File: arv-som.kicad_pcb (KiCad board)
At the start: 2 copper layers, 55 x 40 mm, 345 parts, among them J3 DF40C-100DP-0.4V(51), J4 DF40C-100DP-0.4V(51), Q1 BSS138AKA, Q2 BSS138AKA, Q3 BSS138AKA, Q4 BSS138AKA, U10 TDA19988BHN_C1,557, U11 KSZ9031RNXCA, U12 MT53E256M32D2DS-053, U13 VIC7100, U2 MT53E256M32D2, U5 LMR62014XMF_NOPB, U8 TPS65086100, U9 GD25LQ256DWIGR, Y1 ABM8G-25.000MHZ-18-D2Y-T

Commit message: Renamed design files
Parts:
- SP1, SP2, SP3, SP4: footprint riscv-u74-som-footprints:9774030151 -> arv-som-footprints:9774030151
- U2: footprint riscv-u74-som-footprints:BGA-200_10.0x14.5mm_Layout12x22_P0.80x0.65mm -> arv-som-footprints:BGA-200_10.0x14.5mm_Layout12x22_P0.80x0.65mm
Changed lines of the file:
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@@
     )
   )
-  (module riscv-u74-som-footprints:9774030151 (layer F.Cu)
+  (module arv-som-footprints:9774030151 (layer F.Cu)
     (at 181.520001 91.470002)
     (fp_text reference SP4 (at 0 -4.2) (layer F.SilkS)
@@
     )
   )
-  (module riscv-u74-som-footprints:9774030151 (layer F.Cu)
+  (module arv-som-footprints:9774030151 (layer F.Cu)
     (at 133.520001 91.470002)
     (fp_text reference SP3 (at 0 -4.2) (layer F.SilkS)
@@
     )
   )
-  (module riscv-u74-som-footprints:9774030151 (layer F.Cu)
+  (module arv-som-footprints:9774030151 (layer F.Cu)
     (at 181.520001 58.470002)
     (fp_text reference SP2 (at 0 -4.2) (layer F.SilkS)
@@
     )
   )
-  (module riscv-u74-som-footprints:9774030151 (layer F.Cu)
+  (module arv-som-footprints:9774030151 (layer F.Cu)
     (at 133.520001 58.470002)
     (fp_text reference SP1 (at 0 -4.2) (layer F.SilkS)
@@
     )
   )
-  (module riscv-u74-som-footprints:BGA-200_10.0x14.5mm_Layout12x22_P0.80x0.65mm (layer F.Cu)
+  (module arv-som-footprints:BGA-200_10.0x14.5mm_Layout12x22_P0.80x0.65mm (layer F.Cu)
     (at 175.620001 73.970002)
     (descr "BGA-200, 14.5x10.0mm, 200 Ball, 12x22 Layout, 0.8x0.65mm Pitch, http://www.issi.com/WW/pdf/43-46LQ32256A-AL.pdf")

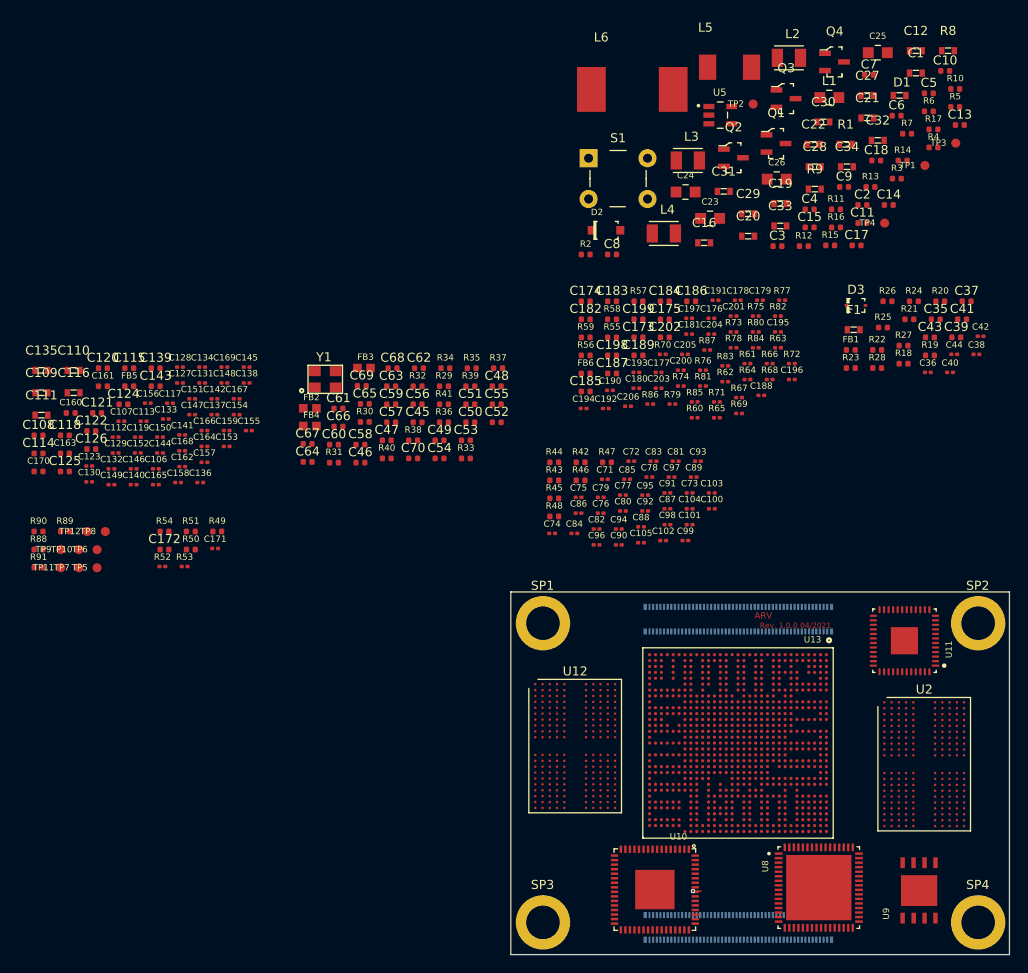
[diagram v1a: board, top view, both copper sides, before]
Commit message: Updated interfaces, CPU and B2B connector connections
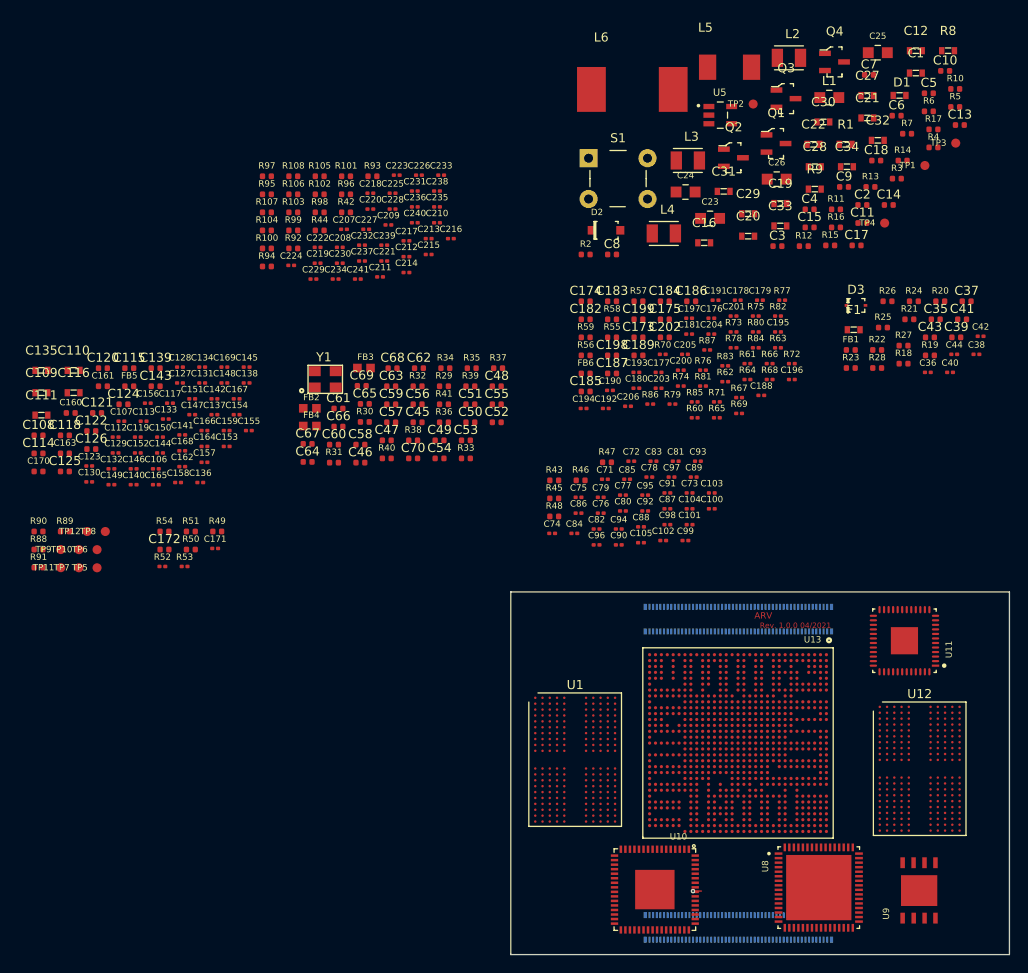
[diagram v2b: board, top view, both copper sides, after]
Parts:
- removed SP1, SP2, SP3, SP4: 9774030151, arv-som-footprints:9774030151
- removed U2: MT53E256M32D2, arv-som-footprints:BGA-200_10.0x14.5mm_Layout12x22_P0.80x0.65mm
- added C207: C_100n_0201, antmicro-footprints:0201-res, F.Cu at (111.6, 15.0)
- added C208: C_100n_0201, antmicro-footprints:0201-res, F.Cu at (111.2, 17.0)
- added C209: C_100n_0201, antmicro-footprints:0201-res, F.Cu at (116.5, 14.5)
- added C210: C_100n_0201, antmicro-footprints:0201-res, F.Cu at (121.9, 14.3)
- added C211: C_100n_0201, antmicro-footprints:0201-res, F.Cu at (115.6, 20.2)
- added C212: C_100n_0201, antmicro-footprints:0201-res, F.Cu at (118.5, 18.0)
- added C213: C_100n_0201, antmicro-footprints:0201-res, F.Cu at (121.0, 16.0)
- added C214: C_100n_0201, antmicro-footprints:0201-res, F.Cu at (118.5, 19.7)
- added C215: C_100n_0201, antmicro-footprints:0201-res, F.Cu at (121.0, 17.8)
- added C216: C_100n_0201, antmicro-footprints:0201-res, F.Cu at (123.4, 16.0)
- added C217: C_100n_0201, antmicro-footprints:0201-res, F.Cu at (118.5, 16.2)
- added C218: C_100n_0201, antmicro-footprints:0201-res, F.Cu at (114.5, 11.0)
- added C219: C_100n_0201, antmicro-footprints:0201-res, F.Cu at (108.7, 18.7)
- added C220: C_100n_0201, antmicro-footprints:0201-res, F.Cu at (114.5, 12.7)
- added C221: C_100n_0201, antmicro-footprints:0201-res, F.Cu at (116.1, 18.5)
- added C222: C_100n_0201, antmicro-footprints:0201-res, F.Cu at (108.7, 17.0)
- added C223: C_100n_0201, antmicro-footprints:0201-res, F.Cu at (117.4, 9.00)
- added C224: C_100n_0201, antmicro-footprints:0201-res, F.Cu at (105.8, 19.0)
- added C225: C_100n_0201, antmicro-footprints:0201-res, F.Cu at (117.0, 11.0)
- added C226: C_100n_0201, antmicro-footprints:0201-res, F.Cu at (119.9, 9.00)
- added C227: C_100n_0201, antmicro-footprints:0201-res, F.Cu at (114.1, 15.0)
- added C228: C_100n_0201, antmicro-footprints:0201-res, F.Cu at (117.0, 12.7)
- added C229: C_100n_0201, antmicro-footprints:0201-res, F.Cu at (108.3, 20.5)
- added C230: C_100n_0201, antmicro-footprints:0201-res, F.Cu at (111.2, 18.7)
- added C231: C_100n_0201, antmicro-footprints:0201-res, F.Cu at (119.4, 10.8)
- added C232: C_100n_0201, antmicro-footprints:0201-res, F.Cu at (113.6, 16.7)
- added C233: C_100n_0201, antmicro-footprints:0201-res, F.Cu at (122.3, 9.00)
- added C234: C_100n_0201, antmicro-footprints:0201-res, F.Cu at (110.7, 20.5)
- added C235: C_100n_0201, antmicro-footprints:0201-res, F.Cu at (121.9, 12.5)
- added C236: C_100n_0201, antmicro-footprints:0201-res, F.Cu at (119.4, 12.5)
- added C237: C_100n_0201, antmicro-footprints:0201-res, F.Cu at (113.6, 18.5)
- added C238: C_100n_0201, antmicro-footprints:0201-res, F.Cu at (121.9, 10.8)
- added C239: C_100n_0201, antmicro-footprints:0201-res, F.Cu at (116.1, 16.7)
- added C240: C_100n_0201, antmicro-footprints:0201-res, F.Cu at (119.4, 14.3)
- added C241: C_100n_0201, antmicro-footprints:0201-res, F.Cu at (113.2, 20.5)
- added R100: R_0R_0402, antmicro-footprints:0402-res, F.Cu at (103.1, 17.1)
- added R101: R_10k_0402, antmicro-footprints:0402-res, F.Cu at (111.9, 9.12)
- added R102: R_0R_0402, antmicro-footprints:0402-res, F.Cu at (108.9, 11.1)
- added R103: R_10k_0402, antmicro-footprints:0402-res, F.Cu at (106.0, 13.1)
- added R104: R_10k_0402, antmicro-footprints:0402-res, F.Cu at (103.1, 15.1)
- added R105: R_10k_0402, antmicro-footprints:0402-res, F.Cu at (108.9, 9.12)
- added R106: R_10k_0402, antmicro-footprints:0402-res, F.Cu at (106.0, 11.1)
- added R107: R_10k_0402, antmicro-footprints:0402-res, F.Cu at (103.1, 13.1)
- added R108: R_10k_0402, antmicro-footprints:0402-res, F.Cu at (106.0, 9.12)
- added R92: R_10k_0402, antmicro-footprints:0402-res, F.Cu at (106.0, 17.1)
- added R93: R_10k_0402, antmicro-footprints:0402-res, F.Cu at (114.8, 9.12)
- added R94: R_10k_0402, antmicro-footprints:0402-res, F.Cu at (103.1, 19.1)
- added R95: R_10k_0402, antmicro-footprints:0402-res, F.Cu at (103.1, 11.1)
- added R96: R_10k_0402, antmicro-footprints:0402-res, F.Cu at (111.9, 11.1)
- added R97: R_240R_0402, antmicro-footprints:0402-res, F.Cu at (103.1, 9.12)
- added R98: R_10k_0402, antmicro-footprints:0402-res, F.Cu at (108.9, 13.1)
- added R99: R_240R_0402, antmicro-footprints:0402-res, F.Cu at (106.0, 15.1)
- added U1: MT53E256M32D2DS-053, antmicro-footprints:BGA-200_10.0x14.5mm_Layout12x22_P0.80x0.65mm, F.Cu at (137.1, 73.5)
- R42: value R_10k_0402 -> R_240R_0402
- moved U12 38.1 mm to (175.1, 74.5)
- moved R42 37.8 mm to (111.9, 13.1)
- moved R44 36.4 mm to (108.9, 15.1)
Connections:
- net ETH_INT_N renamed Net-(U11-Pad38)
- net ETH_MDC renamed RGMII_MDC
- net ETH_nLED1 renamed Net-(J3-Pad19)
- net FNSH028_HDMI_I2S_TX0 renamed HDMI_I2S_TX0
- net Net-(R44-Pad2) renamed DDR0_ODT_1
- net RGMII_REF_CLK renamed LED_MODE
- net RGMII_RX_CLK renamed RGMII_RXCLK
- net RGMII_RX_DV renamed RGMII_RXDV
- net RGMII_TX_CLK renamed RGMII_GTXCLK
- net SYNC_IN renamed Net-(J3-Pad16)
- net SYNC_OUT renamed Net-(J3-Pad18)
- J4 pad 57: DSI0_D0_N -> CDTX_DSI_D0_N
- J4 pad 59: DSI0_D0_P -> CDTX_DSI_D0_P
- J4 pad 63: DSI0_D1_N -> CDTX_DSI_D1_N
- J4 pad 65: DSI0_D1_P -> CDTX_DSI_D1_P
- J4 pad 69: DSI0_C_N -> CDTX_DSI_D2_N
- J4 pad 71: DSI0_C_P -> CDTX_DSI_D2_P
- R39 pad 1: ETH_LED1 -> ETH_LED2
- R40 pad 1: ETH_LED2 -> ETH_LED1
- R42 pad 1: CS0_B -> Net-(R42-Pad1)
- R42 pad 2: GND -> VDDQ
- R45 pad 2: GND -> VDDQ
- R46 pad 2: OTD_CA_A -> DDR0_ODT_0
- R48 pad 2: RESET_N -> DDR0_RSTN
- U10 pad 23: FNSH026_HDMI_BCLK -> HDMI_BCLK
- U10 pad 24: FNSH027_HDMI_I2S_LRCLK -> HDMI_LRCLK
- U10 pad 27: FNSH025_HDMI_12MHZ -> HDMI_12MHZ
- U10 pad 50: FNSH032_HDMI_INT -> HDMI_INT
- U10 pad 51: FNSH061_I2C0_SDA -> I2C0_SDA
- U10 pad 52: FNSH062_I2C0_SCL -> I2C0_SCL
- U11 pad 25: RGMII_TX_DV -> RGMII_TXEN
- U11 pad 37: ETH_MDIO -> RGMII_MDIO
- U12 pad A8: Net-(U12-PadA8) -> Net-(R42-Pad1)
- U12 pad AA11: Net-(U12-PadAA11) -> DDR0_DQ24
- U12 pad AA2: Net-(U12-PadAA2) -> DDR0_DQ16
- U12 pad AA4: Net-(U12-PadAA4) -> DDR0_DQ23
- U12 pad AA9: Net-(U12-PadAA9) -> DDR0_DQ31
- U12 pad B11: DQ08_A -> DDR0_DQ08
- U12 pad B2: DQ00_A -> DDR0_DQ00
- U12 pad B4: DQ07_A -> DDR0_DQ07
- U12 pad B9: DQ15_A -> DDR0_DQ15
- U12 pad C10: DMI_1A -> DDR0_DMI1
- U12 pad C11: DQ09_A -> DDR0_DQ09
- U12 pad C2: DQ01_A -> DDR0_DQ01
- U12 pad C3: DMI_0A -> DDR0_DMI0
- U12 pad C4: DQ06_A -> DDR0_DQ06
- U12 pad C9: DQ14_A -> DDR0_DQ14
- U12 pad D10: DQ_S1_TA -> DDR0_DQS1N
- U12 pad D3: DQ_S0_TA -> DDR0_DQS0N
- U12 pad E10: DQ_S1_CA -> DDR0_DQS1P
- U12 pad E11: DQ10_A -> DDR0_DQ10
- U12 pad E2: DQ02_A -> DDR0_DQ02
- U12 pad E3: DQ_S0_CA -> DDR0_DQS0P
- U12 pad E4: DQ05_A -> DDR0_DQ05
- U12 pad E9: DQ13_A -> DDR0_DQ13
- U12 pad F11: DQ11_A -> DDR0_DQ11
- U12 pad F2: DQ03_A -> DDR0_DQ03
- U12 pad F4: DQ04_A -> DDR0_DQ04
- U12 pad F9: DQ12_A -> DDR0_DQ12
- U12 pad H3: Net-(U12-PadH3) -> DDR0_CS1
- U12 pad H4: CS0_A -> DDR0_CS0
- U12 pad J5: Net-(U12-PadJ5) -> DDR0_CKE1
- U12 pad P4: DDR0_CKE1 -> DDR0_CKE0
- U12 pad P5: Net-(U12-PadP5) -> DDR0_CKE1
- U12 pad R3: Net-(U12-PadR3) -> DDR0_CS3
- U12 pad R4: CS0_B -> DDR0_CS2
- U12 pad U11: Net-(U12-PadU11) -> DDR0_DQ27
- U12 pad U2: Net-(U12-PadU2) -> DDR0_DQ19
- U12 pad U4: Net-(U12-PadU4) -> DDR0_DQ20
- U12 pad U9: Net-(U12-PadU9) -> DDR0_DQ28
- U12 pad V10: Net-(U12-PadV10) -> DDR0_DQS3P
- U12 pad V11: Net-(U12-PadV11) -> DDR0_DQ26
- U12 pad V2: Net-(U12-PadV2) -> DDR0_DQ18
- U12 pad V3: Net-(U12-PadV3) -> DDR0_DQS2P
- U12 pad V4: Net-(U12-PadV4) -> DDR0_DQ21
- U12 pad V9: Net-(U12-PadV9) -> DDR0_DQ29
- U12 pad W10: Net-(U12-PadW10) -> DDR0_DQS3N
- U12 pad W3: Net-(U12-PadW3) -> DDR0_DQS2N
- U12 pad Y10: Net-(U12-PadY10) -> DDR0_DMI3
- U12 pad Y11: Net-(U12-PadY11) -> DDR0_DQ25
- U12 pad Y2: Net-(U12-PadY2) -> DDR0_DQ17
- U12 pad Y3: Net-(U12-PadY3) -> DDR0_DMI2
- U12 pad Y4: Net-(U12-PadY4) -> DDR0_DQ22
- U12 pad Y9: Net-(U12-PadY9) -> DDR0_DQ30
- U13 pad AB30: GMAC_TXEN -> RGMII_TXEN
- U13 pad Y29: ETH_MDIO -> RGMII_MDIO

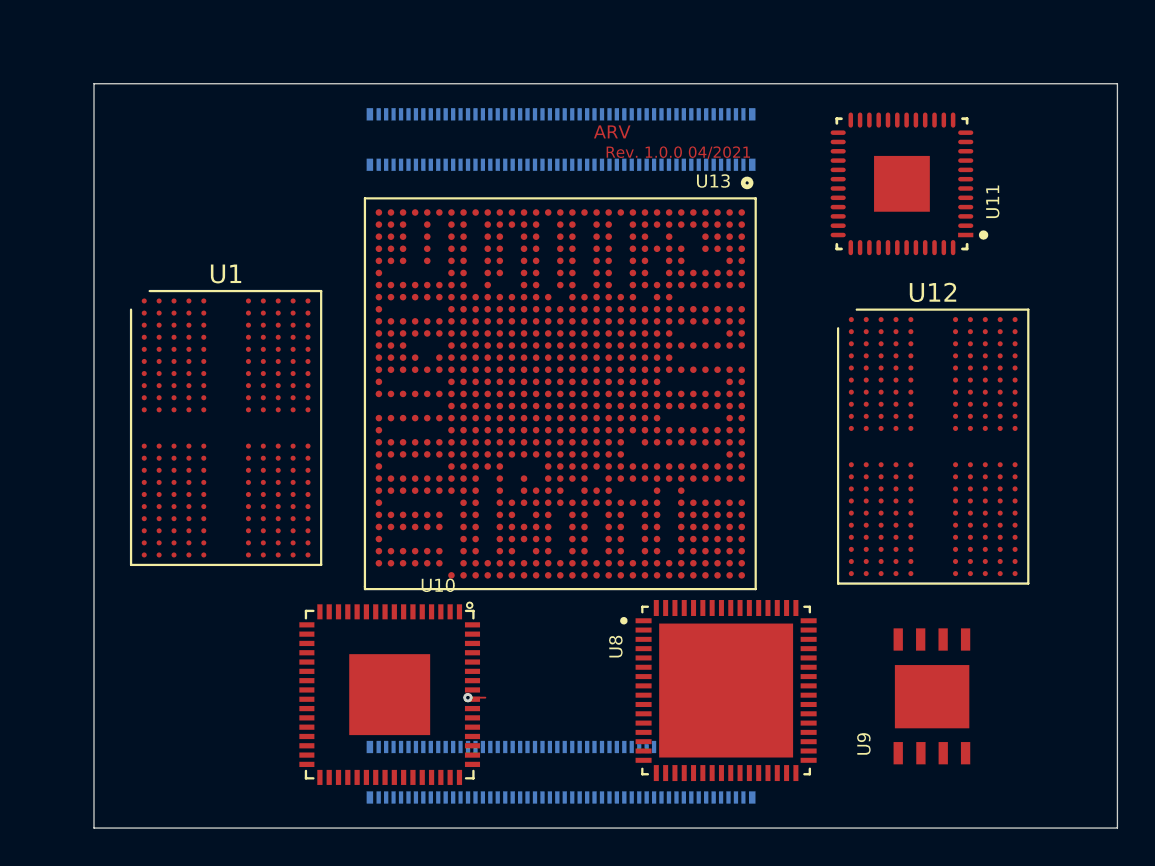
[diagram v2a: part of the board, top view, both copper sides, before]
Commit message: Added logotypes
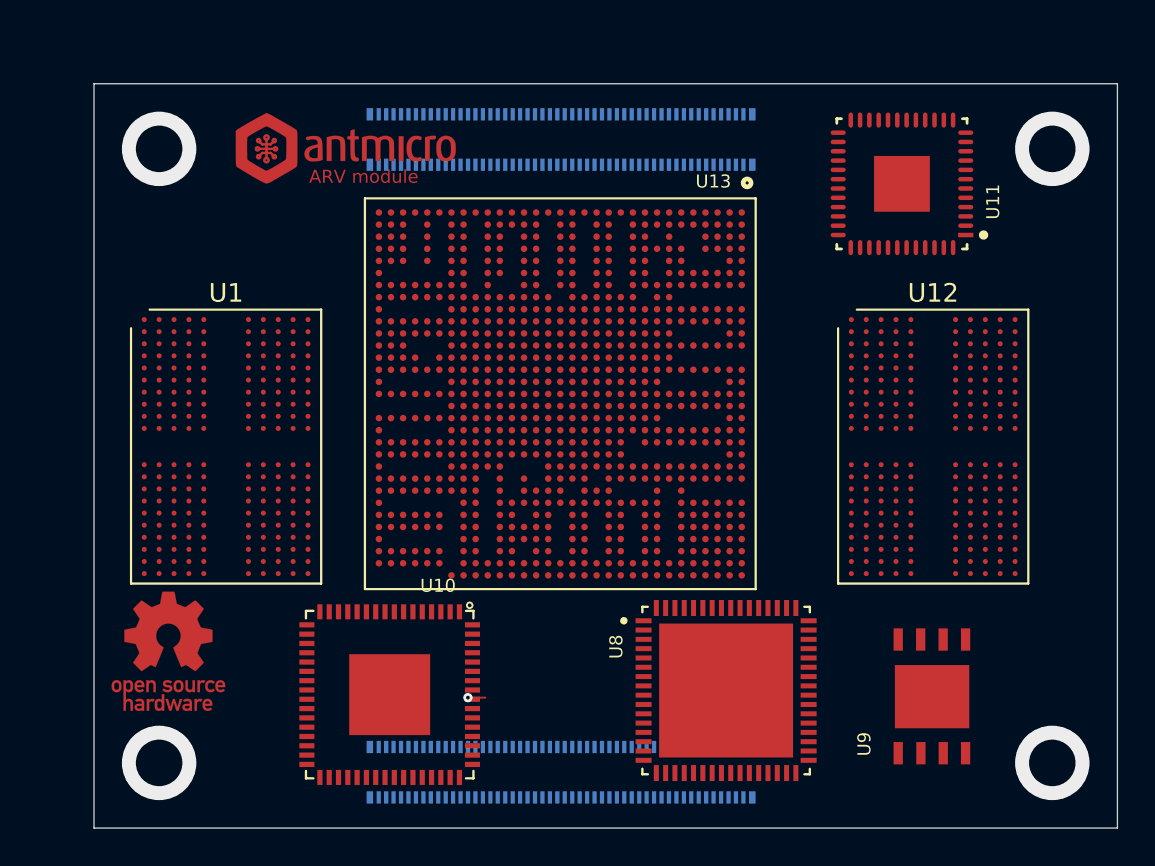
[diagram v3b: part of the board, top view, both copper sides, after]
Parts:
- added N1: antmicro_logo, antmicro-footprints:antmicro-logo_scaled_12mm, F.Cu at (143.5, 58.5)
- added N2: oshw_logo, antmicro-footprints:oshw-logo, F.Cu at (134.0, 85.5)
- moved U1 1.00 mm to (137.1, 74.5)
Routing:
- net (no net): vias 0 -> 4
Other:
- board text added: "ARV module"
- board text removed: "ARV"
- board text removed: "Rev. 1.0.0 04/2021"

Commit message: Minor mock update
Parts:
- removed C1, C16, C27, C28: C_10u_0603, antmicro-footprints:0603-cap
- removed C10, C13, C17, C18: C_100n_0402_16V, antmicro-footprints:0402-cap
- removed C100, C101, C102, C103, C104, C105, C106, C107, C112, C113, C117, C119, C123, C127, C128, C129, C130, C131, C132, C133, C134, C136, C137, C138, C140, C141, C142, C144, C145, C146, C147, C148, C149, C150, C151, C152, C153, C154, C155, C156, C157, C158, C159, C162, C164, C165, C166, C167, C168, C169, C171, C176, C177, C178, C179, C180, C181, C188, C190, C191, C192, C193, C194, C195, C196, C197, C200, C201, C203, C204, C205, C206, C207, C208, C209, C210, C211, C212, C213, C214, C215, C216, C217, C218, C219, C220, C221, C222, C223, C224, C225, C226, C227, C228, C229, C230, C231, C232, C233, C234, C235, C236, C237, C238, C239, C240, C241, C36, C38, C40, C42, C44, C71, C72, C73, C74, C75, C76, C77, C78, C79, C80, C81, C82, C83, C84, C85, C86, C87, C88, C89, C90, C91, C92, C93, C94, C95, C96, C97, C98, C99: C_100n_0201, antmicro-footprints:0201-res
- removed C108, C124, C125, C126, C143, C173, C174, C175, C183, C185, C186, C187, C189, C198, C199, C202, C35: C_1u_0402, antmicro-footprints:0402-cap
- removed C109, C110, C111, C116, C135, C19, C20, C21, C22, C29, C30, C31, C32, C33, C34: C_22u_0603, antmicro-footprints:0603-cap
- removed C11, C14, C45, C47, C49, C50, C58, C6: C_4u7_0402, antmicro-footprints:0402-cap
- removed C114, C115, C118, C120, C121, C122, C139, C182, C184: C_10u_0402, antmicro-footprints:0402-cap
- removed C12: C_1n_0603, antmicro-footprints:0603-cap
- removed C15, C2, C3, C37, C39, C4, C41, C43, C5, C7, C8, C9: C_2u2_0402, antmicro-footprints:0402-cap
- removed C160, C161, C163, C170: C_1n_0402, antmicro-footprints:0402-res
- removed C172, C55, C56, C57, C59, C60, C61, C62, C63, C64, C65, C66, C67, C68: C_10n_0402, antmicro-footprints:0402-cap
- removed C23, C24, C25, C26: C_100u_0805, antmicro-footprints:0805-cap
- removed C46, C48, C51, C52, C53: C_470n_0402, antmicro-footprints:0402-cap
- removed C54: C_100n_0402, antmicro-footprints:0402-cap
- removed C69, C70: C_22p_0402, antmicro-footprints:0402-cap
- removed D1: PGB1010603MR, antmicro-footprints:PGB1010603MR
- removed D2: 1N4148W-TP, antmicro-footprints:SOD-123
- removed D3: 1N4148WS, antmicro-footprints:SOD-323F
- removed F1: 0ZCM0002FF2G, antmicro-footprints:0603-res
- removed FB1, FB5, FB6: BLM15PD121SN1D, antmicro-footprints:0402-res
- removed FB2, FB3, FB4: BLM18AG601SN1D, antmicro-footprints:0603
- removed L1: 10uH, antmicro-footprints:0805-res
- removed L2, L3, L4: LQH32PN1R0NN0L, antmicro-footprints:IND_LQH32PN1R0NN0L
- removed L5: MPX1D0520LR47, antmicro-footprints:MPX1D0520LR47
- removed L6: IHLP4040DZERR56M01, antmicro-footprints:IHLP4040DZERR56M01
- removed Q1, Q2, Q3, Q4: BSS138AKA, antmicro-footprints:SOT-23-3
- removed R1: R_1M_0603, antmicro-footprints:0603-res
- removed R10, R100, R102, R11, R12, R14, R15, R16, R46, R48, R5, R6: R_0R_0402, antmicro-footprints:0402-res
- removed R101, R103, R104, R105, R106, R107, R108, R2, R25, R3, R31, R32, R33, R34, R35, R36, R38, R39, R4, R40, R43, R44, R47, R49, R50, R51, R54, R88, R90, R92, R93, R94, R95, R96, R98: R_10k_0402, antmicro-footprints:0402-res
- removed R13, R17, R21, R37: R_4k7_0402, antmicro-footprints:0402-res
- removed R18, R19, R20, R22, R23, R24, R55, R56, R57, R58, R59: R_33R_0402, antmicro-footprints:0402-res
- removed R26, R27, R29: R_1k_0402, antmicro-footprints:0402-res
- removed R28: R_27k_0402, antmicro-footprints:0402-res
- removed R30: R_12k1_0402, antmicro-footprints:0402-res
- removed R41: R_1M5_0402, antmicro-footprints:0402-res
- removed R42, R45, R89, R91, R97, R99: R_240R_0402, antmicro-footprints:0402-res
- removed R52, R53: R_0R_0201, antmicro-footprints:0201-res
- removed R60, R61, R62, R63, R64, R65, R66, R67, R68, R69, R70, R71, R72, R73, R74, R75, R76, R77, R78, R79, R80, R81, R82, R83, R84, R85, R86, R87: R_33R_0201, antmicro-footprints:0201-res
- removed R7: R_2k2_0402, antmicro-footprints:0402-res
- removed R8: R_549k_0603, antmicro-footprints:0603-res
- removed R9: R_13k3_0603, antmicro-footprints:0603-res
- removed S1: B3F-1000, antmicro-footprints:Switch_Tactile_THT_B3F-1xxx
- removed TP1, TP10, TP11, TP12, TP2, TP3, TP4, TP5, TP6, TP7, TP8, TP9: TP_SMD1MM, antmicro-footprints:Testpoint_smd_1mm
- removed U5: LMR62014XMF_NOPB, antmicro-footprints:SOT95P280X145-5N
- removed Y1: ABM8G-25.000MHZ-18-D2Y-T, antmicro-footprints:KX-7
- moved U1 0.10 mm to (137.0, 74.5), turned to 180 degrees
- turned U12 to 180 degrees
- turned U8 to 180 degrees
